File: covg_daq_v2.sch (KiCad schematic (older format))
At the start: 29 parts, among them J1 HDMI_A, J10 Conn_02x07_Odd_Even, J11 Conn_02x17_Counter_Clockwise, J2 HDMI_A, J7 HDMI_A, J8 HDMI_A, J9 Conn_02x10_Odd_Even

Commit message: reduced connections to ADC and DAC output headers
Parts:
- J11: value Conn_02x17_Counter_Clockwise -> Conn_02x12_Odd_Even; footprint covg-kicad:PinHeader_2x17_P2.00mm_Horizontal -> covg-kicad:PinHeader_2x12_P2.00mm_Horizontal; symbol Connector_Generic:Conn_02x17_Counter_Clockwise -> Connector_Generic:Conn_02x12_Odd_Even; Manf# SBH21-NBPN-D17-RA-BK -> SBH21-NBPN-D12-RA-BK
- J9: value Conn_02x10_Odd_Even -> Conn_02x06_Odd_Even; symbol Connector_Generic:Conn_02x10_Odd_Even -> Connector_Generic:Conn_02x06_Odd_Even; Manf# SBH21-NBPN-D10-RA-BK -> SBH21-NBPN-D06-RA-BK
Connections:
- net labels added: DAC1_OUT[4..7], DAC2_BP_OUT[4..5], DAC2_BP_OUT[6..7], DAC2_CAL[0..1], GP_ADC_IN[11..15], GP_ADC_IN[5..8]
- net labels removed: DAC1_OUT0, DAC1_OUT1, DAC1_OUT2, DAC1_OUT3, DAC2_OUT2, DAC2_OUT3, GP_ADC_IN[0..7], GP_ADC_IN[8..15], XADC_VP, XADC_XN
- wire segments 343 -> 322

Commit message: rolled back to commit b6c4f66 because of rescue libraries
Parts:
- J11: value Conn_02x12_Odd_Even -> Conn_02x17_Counter_Clockwise; footprint covg-kicad:PinHeader_2x12_P2.00mm_Horizontal -> covg-kicad:PinHeader_2x17_P2.00mm_Horizontal; symbol Connector_Generic:Conn_02x12_Odd_Even -> Connector_Generic:Conn_02x17_Counter_Clockwise; Manf# SBH21-NBPN-D12-RA-BK -> SBH21-NBPN-D17-RA-BK
- J9: value Conn_02x06_Odd_Even -> Conn_02x10_Odd_Even; symbol Connector_Generic:Conn_02x06_Odd_Even -> Connector_Generic:Conn_02x10_Odd_Even; Manf# SBH21-NBPN-D06-RA-BK -> SBH21-NBPN-D10-RA-BK
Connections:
- net labels added: DAC1_OUT0, DAC1_OUT1, DAC1_OUT2, DAC1_OUT3, DAC2_OUT2, DAC2_OUT3, GP_ADC_IN[0..7], GP_ADC_IN[8..15], XADC_VP, XADC_XN
- net labels removed: DAC1_OUT[4..7], DAC2_BP_OUT[4..5], DAC2_BP_OUT[6..7], DAC2_CAL[0..1], GP_ADC_IN[11..15], GP_ADC_IN[5..8]
- wire segments 322 -> 343

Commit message: reduce ADC and DAC connections to ease routing
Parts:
- J11: value Conn_02x17_Counter_Clockwise -> Conn_02x12_Odd_Even; footprint covg-kicad:PinHeader_2x17_P2.00mm_Horizontal -> covg-kicad:PinHeader_2x12_P2.00mm_Horizontal; symbol Connector_Generic:Conn_02x17_Counter_Clockwise -> Connector_Generic:Conn_02x12_Odd_Even; Manf# SBH21-NBPN-D17-RA-BK -> SBH21-NBPN-D12-RA-BK
- J9: value Conn_02x10_Odd_Even -> Conn_02x06_Odd_Even; footprint Connector_PinHeader_2.00mm:PinHeader_2x10_P2.00mm_Horizontal -> Connector_PinHeader_2.00mm:PinHeader_2x06_P2.00mm_Horizontal; symbol Connector_Generic:Conn_02x10_Odd_Even -> Connector_Generic:Conn_02x06_Odd_Even; Manf# SBH21-NBPN-D10-RA-BK -> SBH21-NBPN-D06-RA-BK
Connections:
- net labels added: DAC1_OUT[4..7], DAC2_BP_OUT[4..5], DAC2_BP_OUT[6..7], DAC2_CAL[0..1]
- net labels removed: DAC1_OUT0, DAC1_OUT1, DAC1_OUT2, DAC1_OUT3, DAC2_OUT2, DAC2_OUT3, GP_ADC_IN[0..7], GP_ADC_IN[8..15], XADC_VP, XADC_XN
- wire segments 343 -> 319

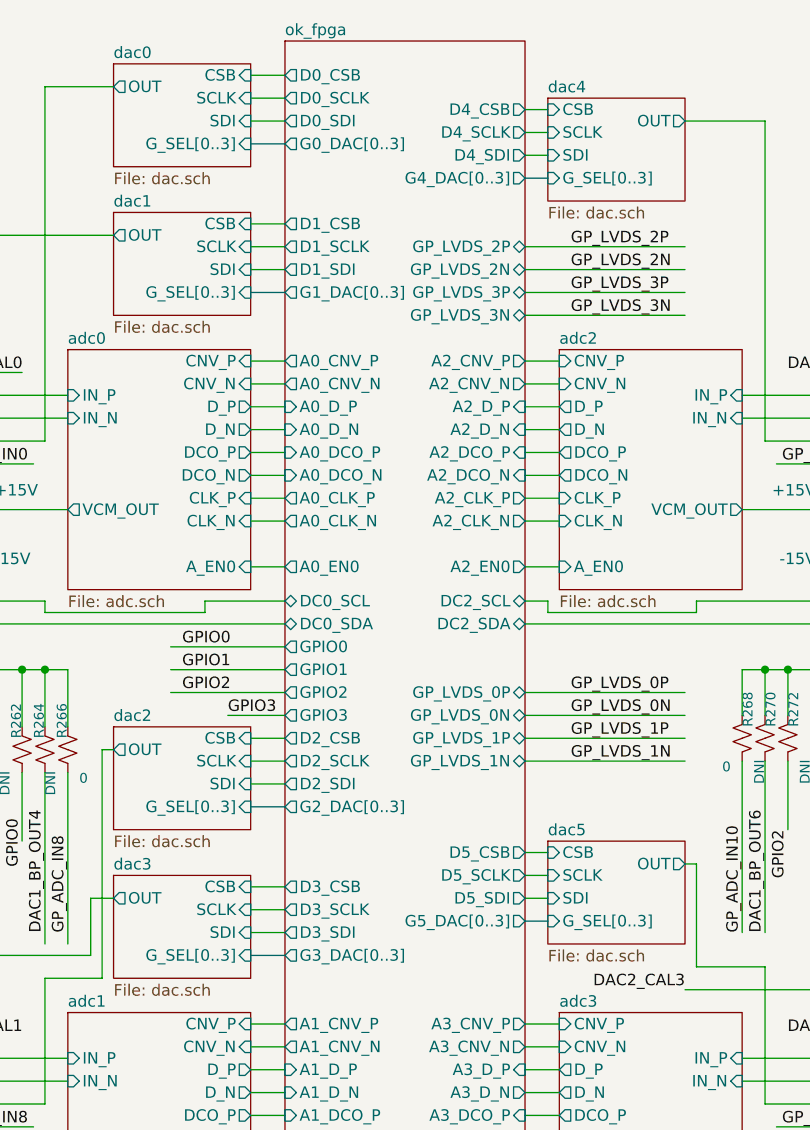
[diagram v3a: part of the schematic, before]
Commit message: move around signals for easier routing
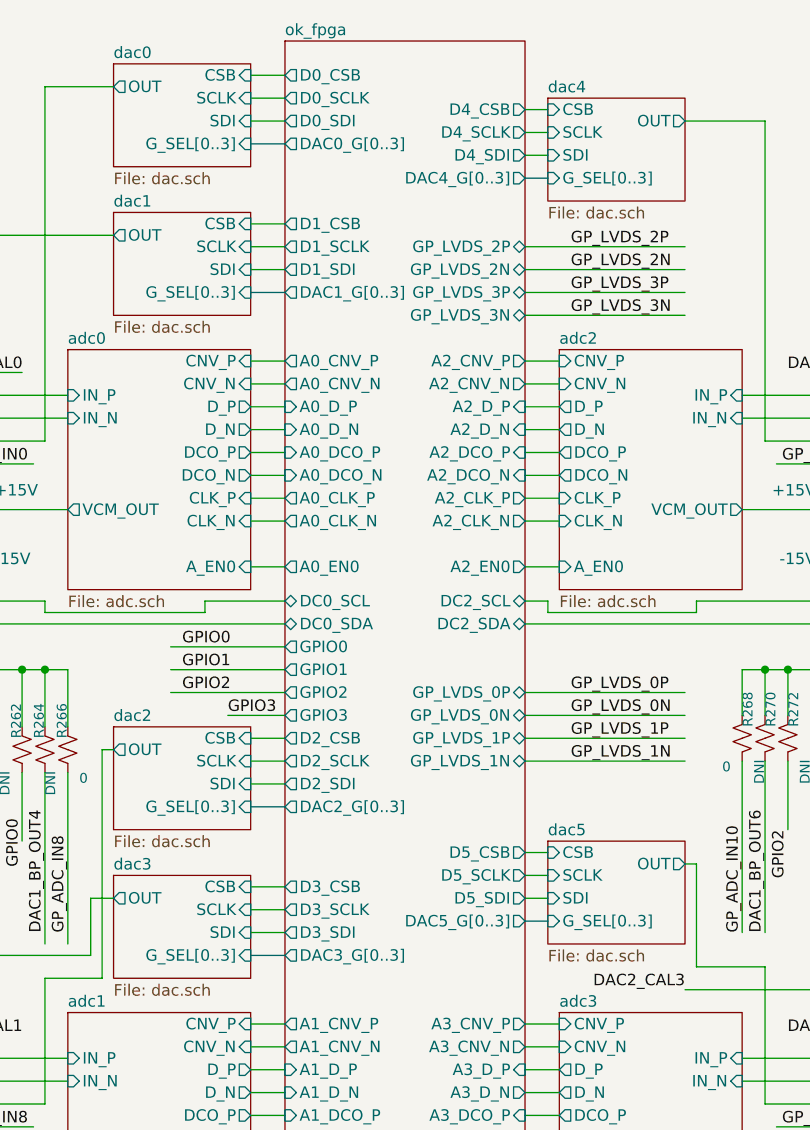
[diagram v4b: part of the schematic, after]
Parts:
- J11: footprint covg-kicad:PinHeader_2x12_P2.00mm_Horizontal -> Connector_PinHeader_2.00mm:PinHeader_2x12_P2.00mm_Horizontal
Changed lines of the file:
@@
 F63 "D5_SCLK" O R 4050 4250 50
 F64 "D5_SDI" O R 4050 4350 50
-F65 "G1_DAC[0..3]" O L 3000 1700 50
-F66 "G0_DAC[0..3]" O L 3000 1050 50
-F67 "G2_DAC[0..3]" O L 3000 3950 50
-F68 "G3_DAC[0..3]" O L 3000 4600 50
-F69 "G5_DAC[0..3]" O R 4050 4450 50
-F70 "G4_DAC[0..3]" O R 4050 1200 50
+F65 "DAC1_G[0..3]" O L 3000 1700 50
+F66 "DAC0_G[0..3]" O L 3000 1050 50
+F67 "DAC2_G[0..3]" O L 3000 3950 50
+F68 "DAC3_G[0..3]" O L 3000 4600 50
+F69 "DAC5_G[0..3]" O R 4050 4450 50
+F70 "DAC4_G[0..3]" O R 4050 1200 50
 F71 "DS2_SDO" I L 3000 7300 50
 F72 "DS2_SCLK" O L 3000 7100 50
@@
 F 0 "J11" H 9950 5950 50  0000 C CNN
 F 1 "Conn_02x12_Odd_Even" H 9950 5850 50  0000 C CNN
-F 2 "covg-kicad:PinHeader_2x12_P2.00mm_Horizontal" H 9900 5200 50  0001 C CNN
+F 2 "Connector_PinHeader_2.00mm:PinHeader_2x12_P2.00mm_Horizontal" H 9900 5200 50  0001 C CNN
 F 3 "~" H 9900 5200 50  0001 C CNN
 F 4 "SBH21-NBPN-D12-RA-BK" H 9900 5200 50  0001 C CNN "Manf#"
